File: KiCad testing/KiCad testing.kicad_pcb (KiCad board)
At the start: 2 copper layers, 101.6 x 127 mm, 45 parts, among them J1 Screw_Terminal_01x02, J2 USB_A, J3 Screw_Terminal_01x02, Q1 IRF540N, Q2 IRF540N, Q3 IRF540N, Q4 IRF540N, U1 IR2113, U2 IR2113

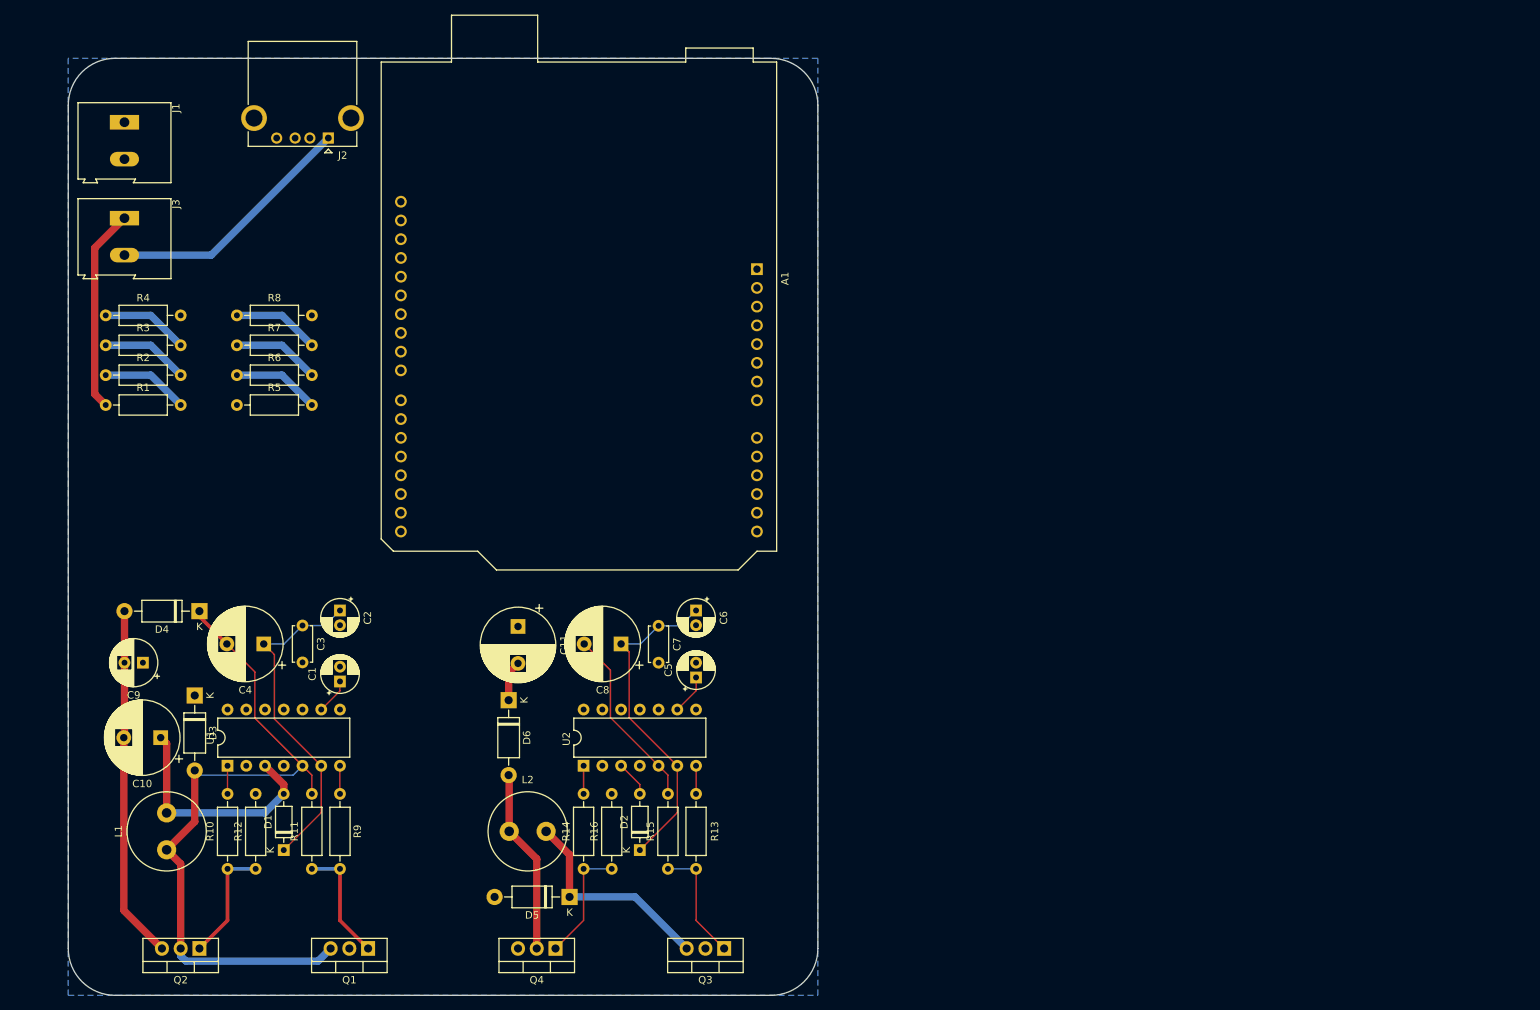
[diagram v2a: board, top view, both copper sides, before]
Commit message: First PCB Final
Here the PCB is fully connected. I do not like the design, but it is fully connected either way. The PCB is still missing the current sensor, as I have no way of knowing what components the small boards we have off amazon are using.

If I had more time, this design would definitely be reworked.
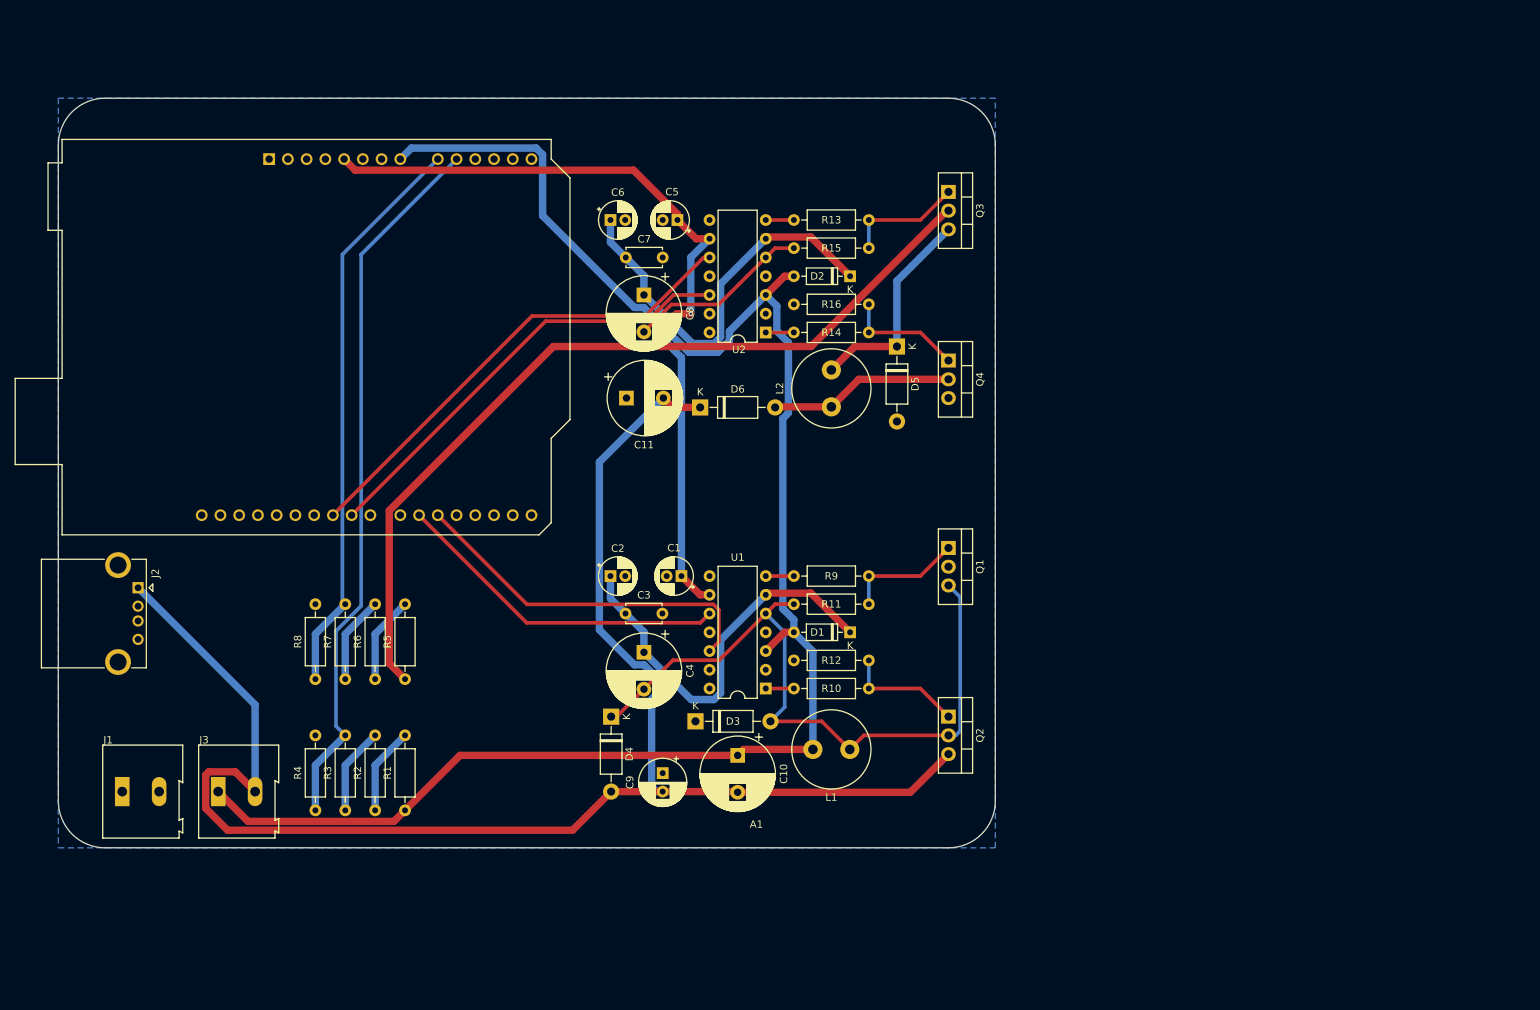
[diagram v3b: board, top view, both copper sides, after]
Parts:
- moved Q3 107.0 mm to (144.7, 43.5), turned to -90 degrees
- moved Q2 106.3 mm to (144.7, 114.6), turned to -90 degrees
- moved Q4 95.8 mm to (144.7, 66.4), turned to -90 degrees
- moved Q1 95.6 mm to (144.7, 91.8), turned to -90 degrees
- moved L1 93.6 mm to (131.3, 119.1), turned to 180 degrees
- moved J1 90.7 mm to (32.7, 124.8), turned to 0 degrees
- moved R10 90.3 mm to (133.9, 110.8), turned to 180 degrees
- moved R15 88.4 mm to (133.9, 51.1), turned to 180 degrees
- moved R12 87.8 mm to (133.9, 107.0), turned to 180 degrees
- moved D5 86.8 mm to (137.7, 64.5), turned to -90 degrees
- moved R16 84.1 mm to (133.9, 58.7), turned to 180 degrees
- moved R11 83.6 mm to (133.9, 99.4), turned to 180 degrees
- moved D2 82.8 mm to (131.4, 54.9), turned to 180 degrees
- moved R14 82.3 mm to (133.9, 62.6), turned to 180 degrees
- moved D1 82.2 mm to (131.4, 103.2), turned to 180 degrees
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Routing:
- net 12V: track 64.8 -> 231.4 mm
- net +Load: track 87.6 -> 220.7 mm
- net +PV: track 0.00 -> 116.4 mm
- net 5V: track 10.3 -> 110.5 mm, vias 0 -> 2
- net Battery_Voltage: track 11.8 -> 97.2 mm
- net PV_Voltage: track 11.8 -> 77.7 mm
- net PWM_MPPT_High: track 0.00 -> 65.5 mm
- net PWM_MPPT_Low: track 0.00 -> 60.9 mm
- net PWM_Low: track 0.00 -> 49.5 mm
- net PWM_High: track 0.00 -> 45.9 mm
- net Net-(D2-K): track 45.2 -> 55.9 mm
- net Net-(D1-K): track 45.5 -> 55.2 mm
- net VS: track 95.3 -> 96.3 mm
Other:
- board size 101.6 x 127 mm -> 127 x 101.6 mm
